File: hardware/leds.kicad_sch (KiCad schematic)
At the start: 28 parts, among them U15 XL-1010RGBC-WS2812B, U16 XL-1010RGBC-WS2812B, U17 XL-1010RGBC-WS2812B, U18 XL-1010RGBC-WS2812B, U22 XL-1010RGBC-WS2812B, U23 XL-1010RGBC-WS2812B, U24 XL-1010RGBC-WS2812B, U25 XL-1010RGBC-WS2812B, U26 XL-1010RGBC-WS2812B, U27 XL-1010RGBC-WS2812B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

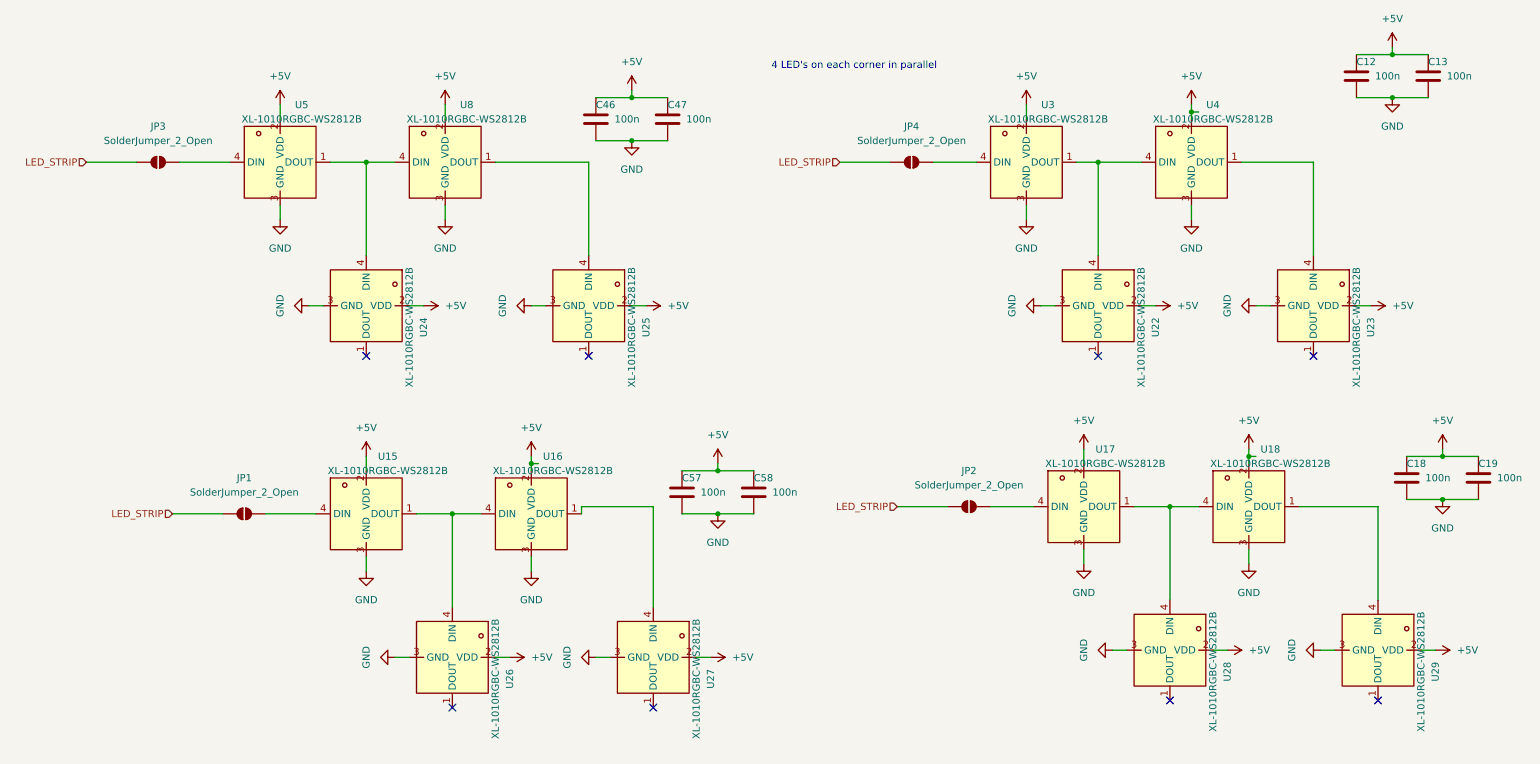
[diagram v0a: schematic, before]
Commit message: switched to 0201
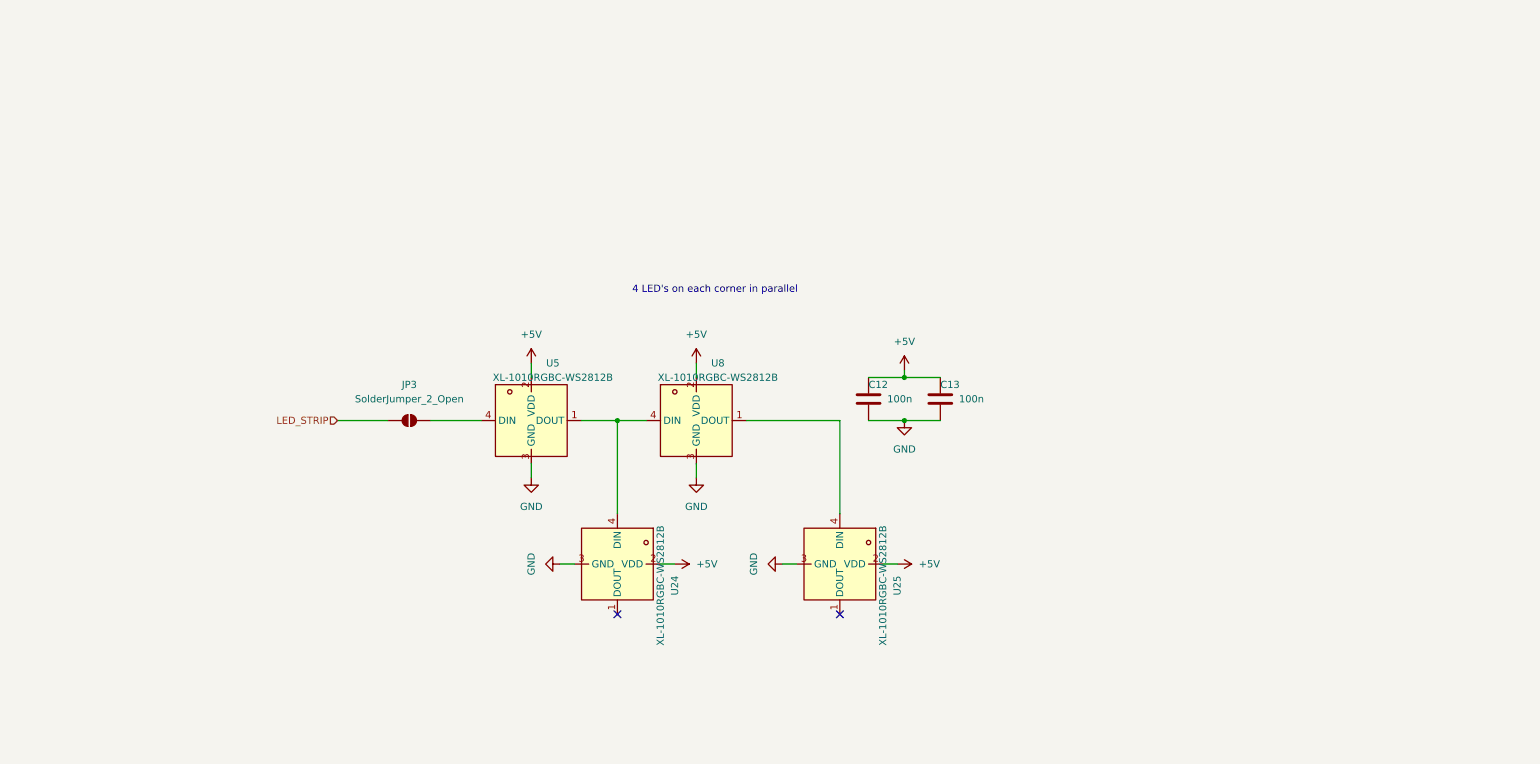
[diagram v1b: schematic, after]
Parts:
- removed C18, C19, C46, C47, C57, C58: 100n, Capacitor_SMD:C_0402_1005Metric, symbol Device:C
- removed JP1, JP2, JP4: SolderJumper_2_Open, Panelization:MouseBite-Slot-Jumper_0201, symbol Jumper:SolderJumper_2_Open
- removed U15, U16, U17, U18, U22, U23, U26, U27, U28, U29, U3, U4: XL-1010RGBC-WS2812B, lib:LED-SMD_4P-L1.0-W1.0-TL_XL-1010RGBC-WS2812B, symbol lib:XL-1010RGBC-WS2812B
- C12, C13: footprint Capacitor_SMD:C_0402_1005Metric -> Capacitor_SMD:C_0201_0603Metric; LCSC C1525 -> C76939
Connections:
- no-connect marks 8 -> 2
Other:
- moved on the sheet: JP3, U24, U25, U5, U8
